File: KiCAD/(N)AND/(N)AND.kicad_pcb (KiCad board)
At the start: 2 copper layers, 71.1 x 62.2 mm, 18 parts, among them J1 Conn_01x02_Pin, J2 Conn_01x02_Pin, J3 Conn_01x02_Pin, J4 Conn_01x02_Pin, Q13 2N7000, Q14 2N7000, Q15 2N7000, Q3 2N7000, Q4 2N7000, Q5 2N7000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

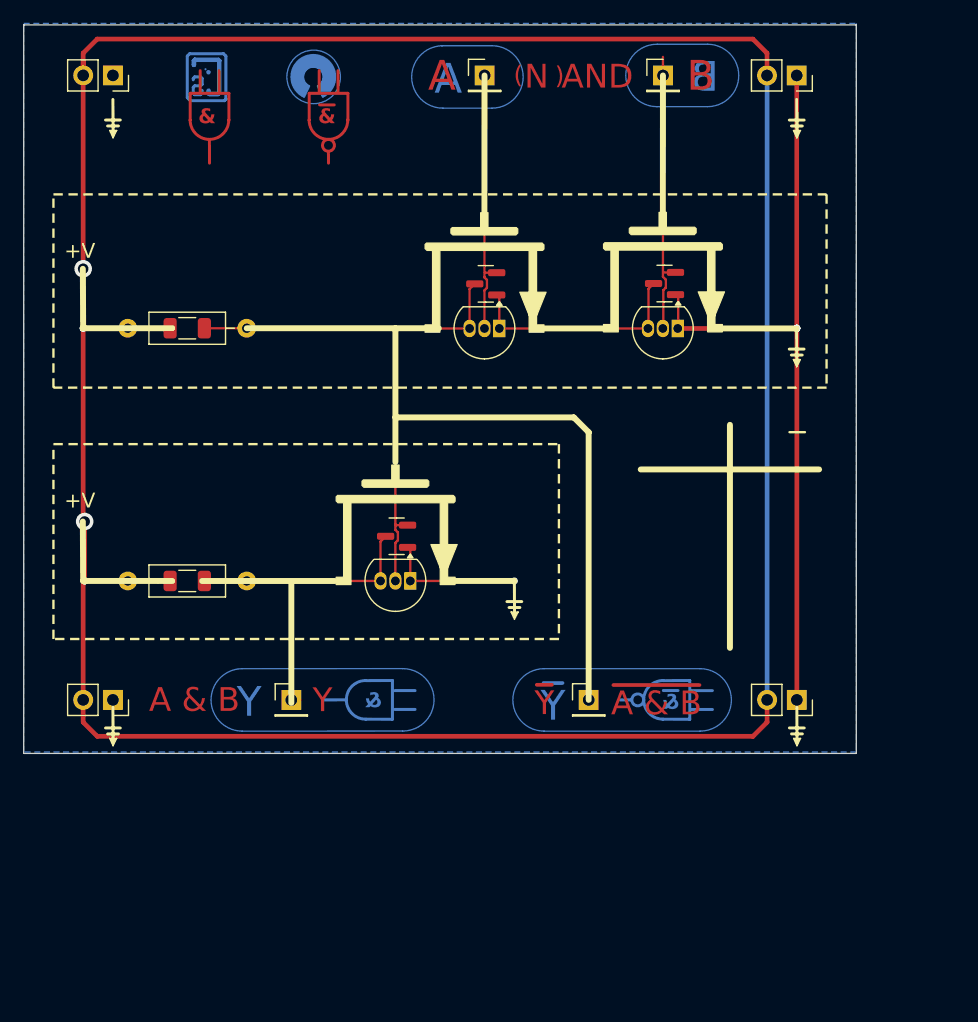
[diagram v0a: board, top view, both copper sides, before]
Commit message: KiCAD: (N)AND_LED
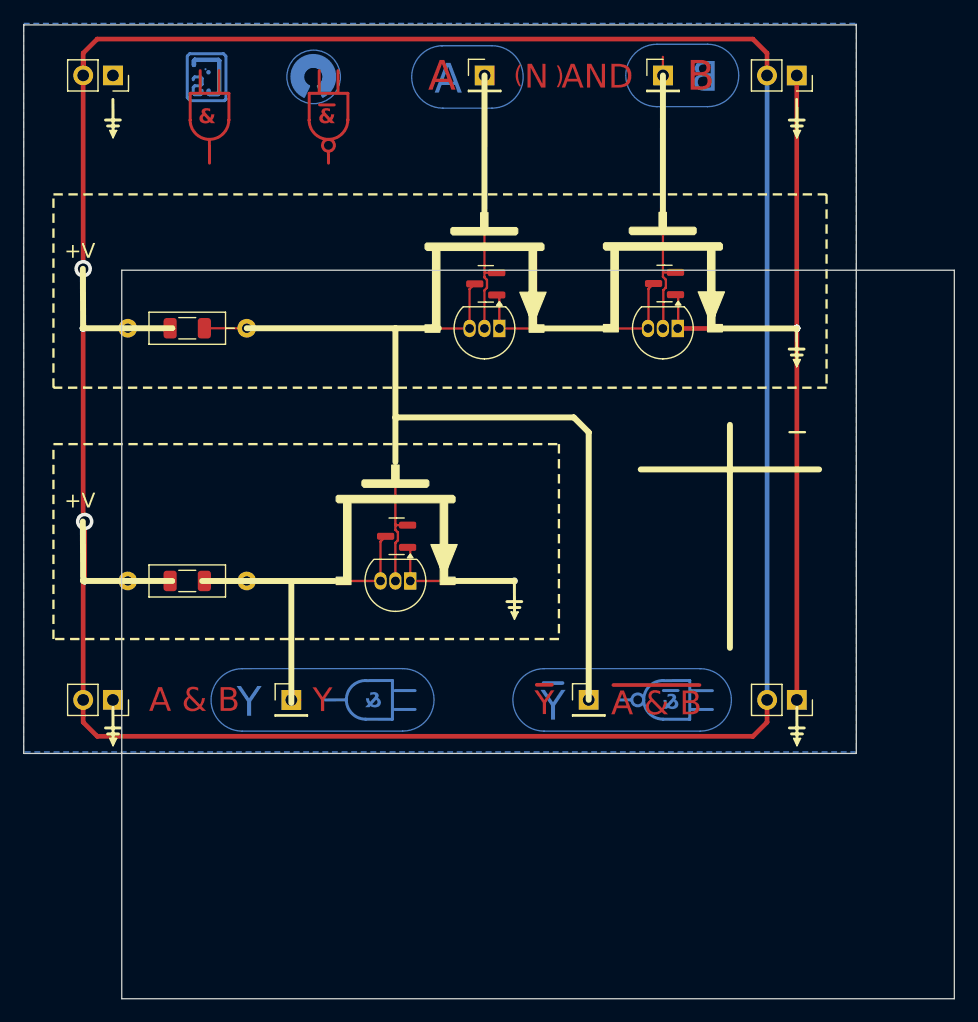
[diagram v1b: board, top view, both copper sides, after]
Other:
- board size 71.1 x 62.2 mm -> 79.5 x 83.2 mm
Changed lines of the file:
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@@
+	)
+	(gr_rect
+		(start 203.199705 111.76)
+		(end 274.319705 173.99)
+		(stroke
+			(width 0.05)
+			(type default)
+		)
+		(fill no)
+		(layer "Edge.Cuts")
 	)
 	(gr_rect
